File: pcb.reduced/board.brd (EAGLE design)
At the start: 127 x 101.6 mm, 28 parts, among them Q1 MPSA42

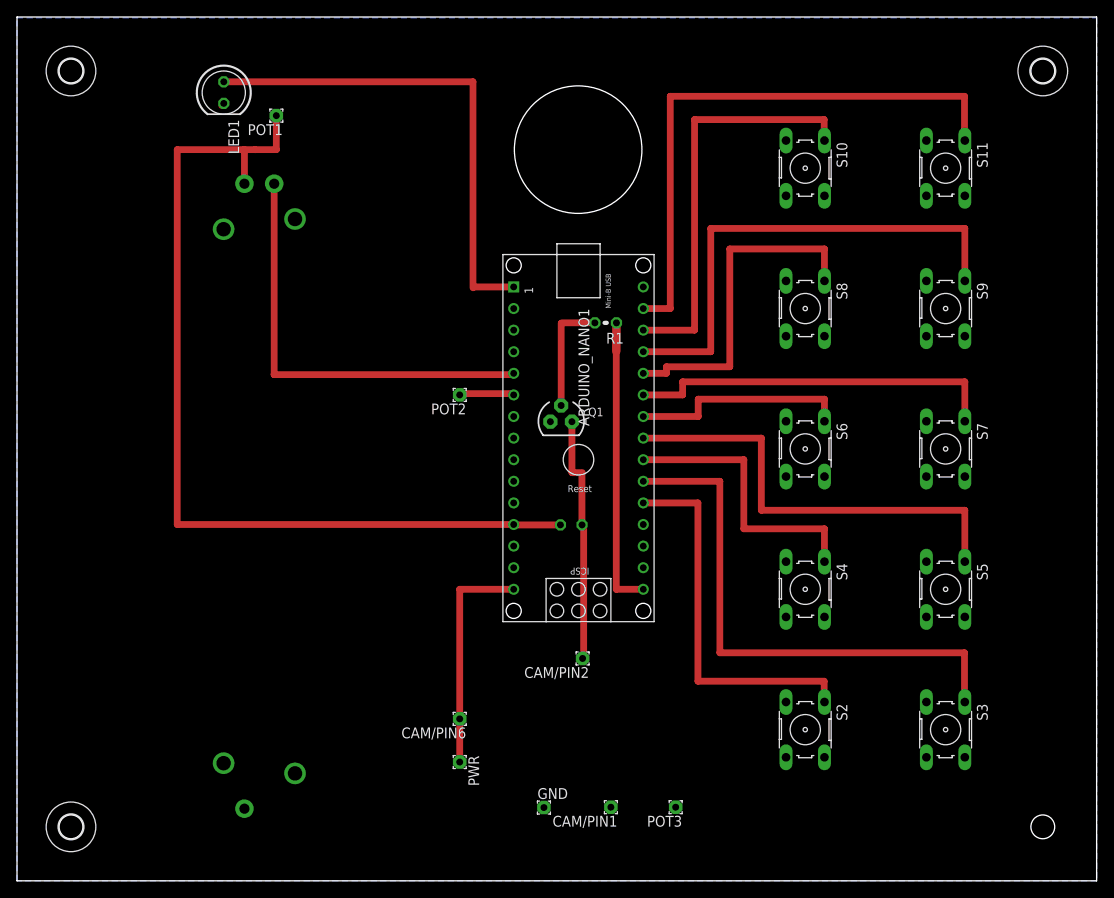
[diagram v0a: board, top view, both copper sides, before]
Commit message: Use bigger buttons and re-layout.
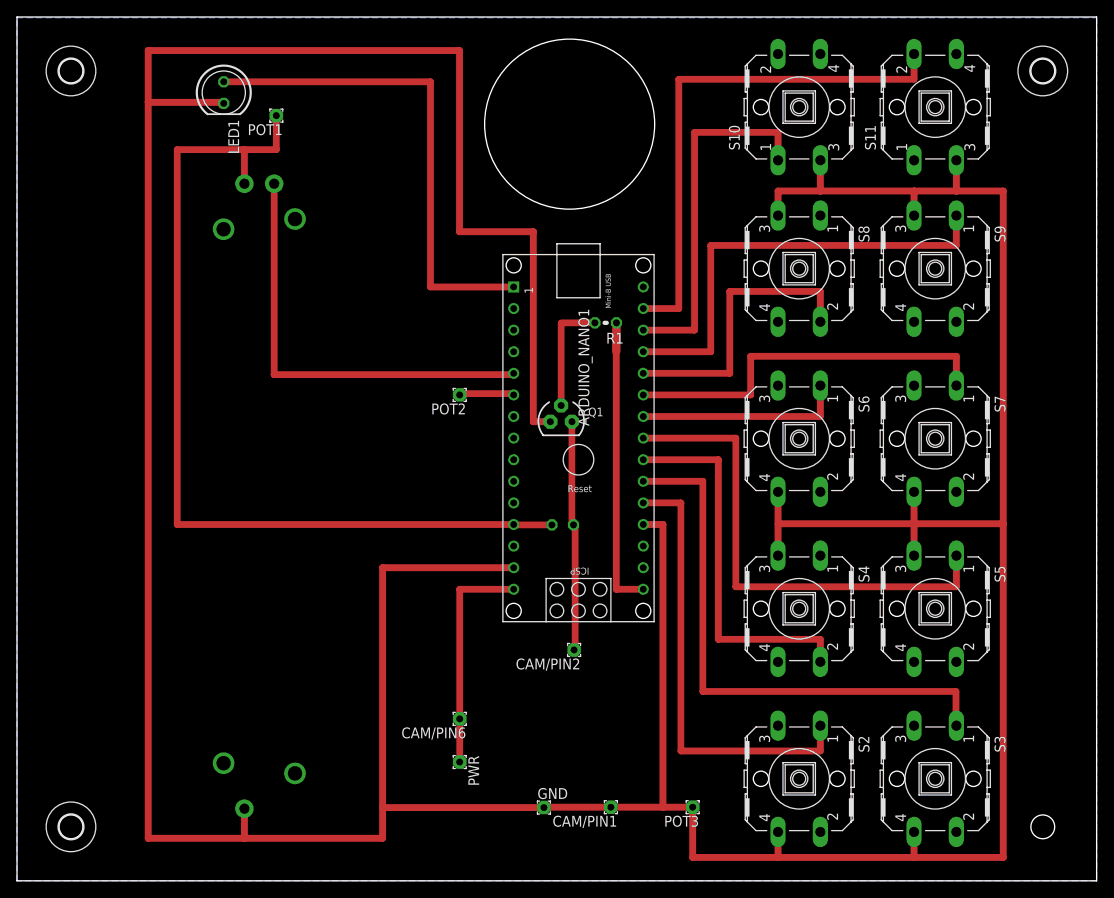
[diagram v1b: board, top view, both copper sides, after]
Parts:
- S10, S11, S2, S3, S4, S5, S6, S7, S8, S9: device switch-omron:B3F-10XX -> switch-omron:B3F-40XX
- moved S11 7.28 mm to (108.0, 91.0), turned to 90 degrees
- moved S10 7.22 mm to (92.0, 91.0), turned to 90 degrees
- moved S3 5.91 mm to (108.0, 12.0)
- moved S2 5.82 mm to (92.0, 12.0)
- moved S9 4.85 mm to (108.0, 72.0)
- moved S8 4.74 mm to (92.0, 72.0)
- moved S5 2.59 mm to (108.0, 32.0)
- moved S4 2.40 mm to (92.0, 32.0)
- moved POT3 2.00 mm to (79.5, 8.66)
- moved S7 1.71 mm to (108.0, 52.0)
- moved CAM/PIN2 1.41 mm to (65.5, 27.2)
- moved S6 1.39 mm to (92.0, 52.0)
- moved R2 1.00 mm to (64.2, 41.9)
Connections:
- net GND: now also S2.4, S3.4, S6.4, S7.4, S8.4; no longer S2.3, S3.3, S6.3, S7.3
- net N$12: now also S11.2; no longer S11.1
- net N$5: now also S4.2; no longer S4.1
- net N$9: now also S8.2; no longer S8.1
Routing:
- net GND: track 0.45 -> 551.2 mm
- net N$5: track 33.3 -> 44.6 mm
- net N$3: track 44.7 -> 53.0 mm
- net N$12: track 67.9 -> 61.8 mm
- net N$11: track 48.5 -> 42.4 mm
- net N$9: track 39.7 -> 34.0 mm
- net N$10: track 58.5 -> 52.8 mm
- net N$6: track 52.3 -> 58.0 mm
- net N$18: track 29.4 -> 27.1 mm
- net N$4: track 63.7 -> 65.5 mm
- net N$7: track 26.0 -> 24.5 mm
- net N$2: track 108.9 -> 107.9 mm
- net N$8: track 44.0 -> 44.8 mm
